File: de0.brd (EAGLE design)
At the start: 150.3 x 89.5 mm, 135 parts, among them IC1 PL2303SA__LF, J2 UX60SC-MB-5ST, U1 P0082, U2 RFM95W-915S2, U3 TPS76201DBVR, U4 TPS76201DBVR, U5 TPS76201DBVR

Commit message: change as Duran's suggest
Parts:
- removed U$48, U$49, U$50, U$51, U$52, U$53: (no value), qfp160:POINT
- added D10, D11, D12, D13, D14: LED0, SparkFun-LED:LED-0603
- added JP1, JP2, JP3: (no value), jumper:JP1
- added Q1, Q2, Q3, Q4, Q5: AS9013-H-HF, SamacSys_Parts:SOT95P240X105-3N
- added R23, R24, R25, R26, R27: 330, SparkFun-Resistors:0603
- added SV3, SV4: (no value), con-lstb:MA06-1
- REG_OUT_33: value REG_OUT_33 -> (none); device jumper:04C -> jumper:JP2Q
- moved C12 26.4 mm to (36.0, 44.2), flipped to the top, turned to 90 degrees
- moved C11 25.5 mm to (34.5, 44.3), flipped to the top, turned to 90 degrees
- moved C13 24.4 mm to (57.6, -3.56), flipped to the top, turned to 270 degrees
- moved C15 24.3 mm to (60.6, -3.55), flipped to the top, turned to 270 degrees
- moved C14 22.7 mm to (59.1, -3.55), flipped to the top, turned to 270 degrees
- moved C16 22.4 mm to (62.1, -3.57), flipped to the top, turned to 270 degrees
- moved C22 19.6 mm to (77.4, 44.1), flipped to the top
- moved C19 19.5 mm to (75.9, 44.1), flipped to the top
- moved REG_OUT_07 6.61 mm to (-22.9, 32.6)
- moved C21 6.07 mm to (59.0, 44.0), flipped to the top
- moved C17 6.03 mm to (60.3, 44.1), flipped to the top
- moved C20 5.95 mm to (61.8, 44.0), flipped to the top
- moved C18 5.48 mm to (63.4, 43.9), flipped to the top
- moved REG_OUT_33 4.58 mm to (-23.0, 13.4), turned to 270 degrees
- moved REG_OUT_12 4.36 mm to (-23.2, 23.4)
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- renumbered S1 to SW2, S2 to SW1, S3 to SW0, S4 to RESET, S5 to SW3, S6 to LOCKED
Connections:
- new net LORA_ANT: SV4.6, U2.9
- new net LORA_DIO1: SV4.2, U2.15
- new net LORA_DIO2: SV4.1, U2.16
- new net LORA_DIO3: SV4.5, U2.11
- new net LORA_DIO4: SV4.4, U2.12
- new net LORA_DIO5: SV3.6, U2.7
- new net N$10: D10.C, Q1.3
- new net N$11: D11.A, R24.1
- new net N$12: D11.C, Q2.3
- new net N$13: D12.A, R25.1
- new net N$14: D12.C, Q3.3
- new net N$15: D13.A, R26.1
- new net N$16: D13.C, Q4.3
- new net N$18: D14.A, R27.1
- new net N$19: D14.C, Q5.3
- new net N$23: JP1.2, R8.2
- new net N$24: JP2.2, R7.2
- new net N$25: JP3.2, R6.2
- new net N$9: D10.A, R23.1
- net GND: now also Q1.2, Q2.2, Q3.2, Q4.2, Q5.2
- net LORA_DIO0: now also JP1.1, SV4.3; no longer R8.2, U$53.1
- net LORA_MISO: now also SV3.1; no longer U$48.1
- net LORA_MOSI: now also SV3.2; no longer U$49.1
- net LORA_NSS: now also JP3.1, SV3.4; no longer R6.2, U$51.1
- net LORA_RESET: now also JP2.1, SV3.5; no longer R7.2, U$52.1
- net LORA_SCK: now also SV3.3; no longer U$50.1
- net OUT_33: now also REG_OUT_33.3; no longer REG_OUT_33.1
- net VCCQ: now also Q3.1
- net VO_07: now also Q4.1
- net VO_12: now also Q5.1
- net VO_33: now also Q1.1, REG_OUT_33.4
- net VO_FPGA_33: now also Q2.1, R23.2, R24.2, R25.2, R26.2, R27.2, REG_OUT_33.1; no longer REG_OUT_33.3
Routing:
- net GND: track 202.4 -> 298.7 mm
- net VO_FPGA_33: track 53.5 -> 0.00 mm
- net ADDRESS_10: track 56.1 -> 4.86 mm
- net VO_33: track 195.1 -> 156.9 mm
- net INTERRUPTS_6: track 123.1 -> 94.5 mm
- net VDDH: track 80.9 -> 58.5 mm, vias 7 -> 8
- net INTERRUPTS_5: track 136.7 -> 114.6 mm
- net VDDLS: track 90.6 -> 72.4 mm
- net VO_12: track 34.0 -> 17.2 mm
- net VCCQ: track 139.6 -> 124.2 mm, vias 13 -> 6
- net VO_07: track 28.3 -> 14.0 mm
- net VBN: track 62.7 -> 49.7 mm
- net OUT_07: track 16.6 -> 5.78 mm
- net LORA_NSS: track 52.8 -> 43.7 mm
- net ADDRESS_11: track 59.8 -> 51.6 mm
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- removed copper zone on layer 1, net GND
- removed copper zone on layer 16, net GND
- removed copper zone on layer 1, net OUT_07
- removed copper zone on layer 1, net OUT_12
- removed copper zone on layer 1, net OUT_33
- removed copper zone on layer 1, net VO_07

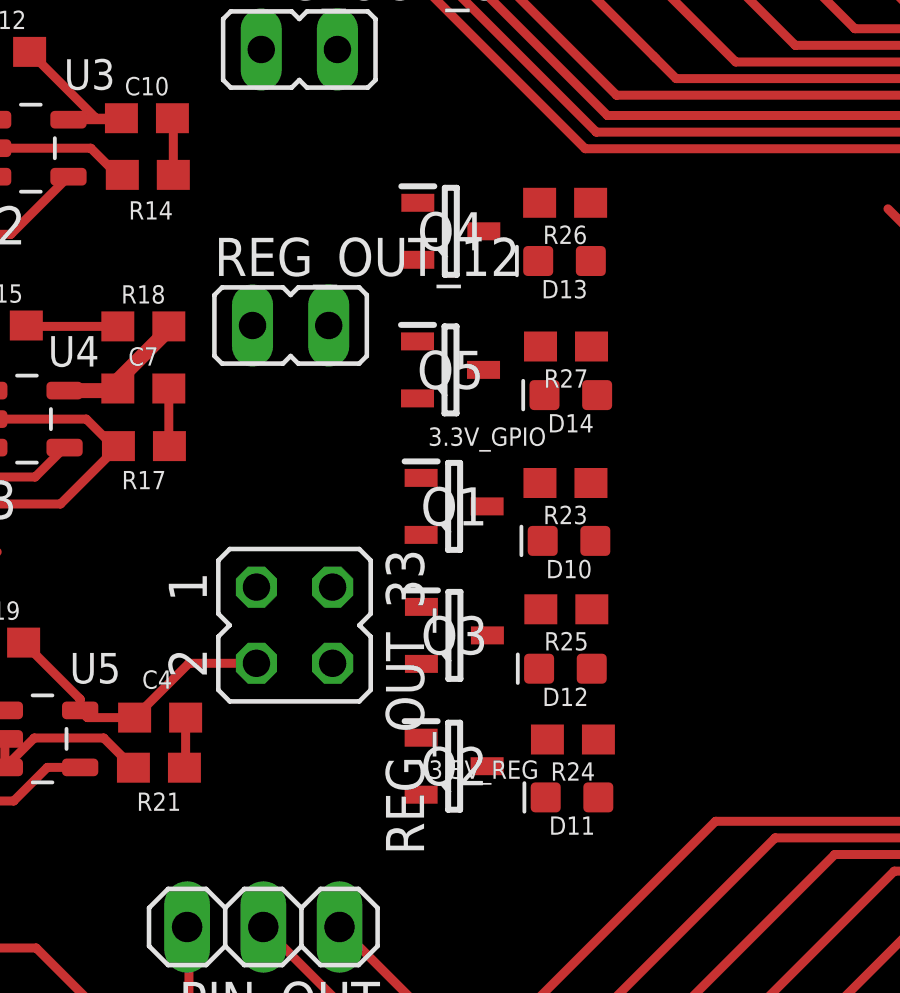
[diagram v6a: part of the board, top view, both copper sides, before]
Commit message: change BJT to MOSFET for power leds
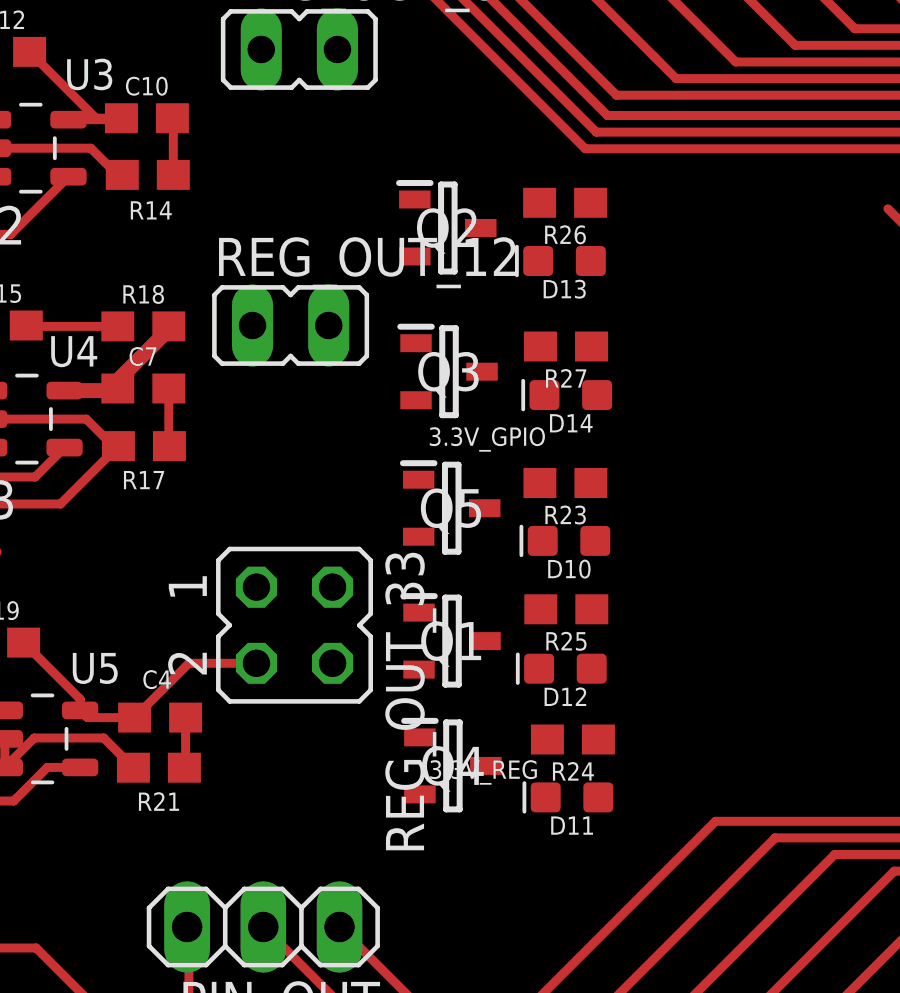
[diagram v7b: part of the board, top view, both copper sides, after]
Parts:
- Q1, Q2, Q3, Q4, Q5: value AS9013-H-HF -> BSH103,235; device SamacSys_Parts:SOT95P240X105-3N -> SamacSys_Parts:SOT95P230X110-3N
- moved Q2 17.9 mm to (-17.9, 26.6)
- moved Q4 17.8 mm to (-17.8, 8.72)
- moved Q3 8.79 mm to (-17.9, 21.9)
- moved Q5 4.61 mm to (-17.8, 17.3)
- moved Q1 4.49 mm to (-17.8, 12.9)
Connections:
- net N$10: now also Q5.3; no longer Q1.3
- net N$12: now also Q4.3; no longer Q2.3
- net N$14: now also Q1.3; no longer Q3.3
- net N$16: now also Q2.3; no longer Q4.3
- net N$19: now also Q3.3; no longer Q5.3
- net OUT_33: now also Q5.1
- net VCCQ: now also Q1.1; no longer Q3.1
- net VO_07: now also Q3.1; no longer Q4.1
- net VO_12: now also Q2.1; no longer Q5.1
- net VO_33: no longer Q1.1
- net VO_FPGA_33: now also Q4.1; no longer Q2.1

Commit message: Update again with Duran's suggest
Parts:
- removed JP1, JP2, JP3: (no value), jumper:JP1
- removed REG_OUT_07: REG_OUT_07, jumper:JP1
- added H1, H2, H3, H4: MOUNT-HOLE3.3, holes:3,3
- added J1: (no value), SparkFun-Connectors:1X02
- added LORA_DIO0, LORA_NSS, LORA_RESET: (no value), jumper:JP1
- added OUT_07: REG_OUT_07, jumper:JP1
- moved C11 32.3 mm to (17.4, 16.8), turned to 180 degrees
- moved C12 31.8 mm to (17.4, 18.4), turned to 180 degrees
- moved C13 21.1 mm to (36.6, -5.23)
- moved C14 21.1 mm to (38.1, -5.22)
- moved C15 20.2 mm to (40.4, -5.22)
- moved C16 20.2 mm to (41.9, -5.24)
- moved Q4 15.6 mm to (-10.8, 22.6)
- moved Q2 15.3 mm to (-10.7, 13.2)
- moved Q5 12.0 mm to (-10.7, 27.0)
- moved D10 10.8 mm to (-6.86, 8.02)
- moved R23 10.8 mm to (-6.98, 9.95)
- moved LOCKED 9.65 mm to (40.8, -31.8)
- moved RESET 9.53 mm to (48.4, -31.8)
- moved R27 8.95 mm to (-6.83, 28.1)
- moved D12 8.70 mm to (-6.76, 16.8)
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- renumbered 5V_JUMPER to 5V, REG_IN_07 to IN_07, REG_IN_12 to IN_12, REG_IN_33 to IN_33, REG_OUT_12 to OUT_12, REG_OUT_33 to OUT_33, UART_JUMPER to UART
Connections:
- net LOCKED: now also J1.1
- net LORA_DIO0: now also LORA_DIO0.1; no longer JP1.1
- net LORA_NSS: now also LORA_NSS.1; no longer JP3.1
- net LORA_RESET: now also LORA_RESET.1; no longer JP2.1
- net N$10: now also Q1.3; no longer Q5.3
- net N$12: now also D12.C, Q3.3; no longer D11.C, Q4.3
- net N$14: now also D11.C, Q2.3; no longer D12.C, Q1.3
- net N$16: now also Q4.3; no longer Q2.3
- net N$19: now also Q5.3; no longer Q3.3
- net N$23: now also LORA_DIO0.2; no longer JP1.2
- net N$24: now also LORA_RESET.2; no longer JP2.2
- net N$25: now also LORA_NSS.2; no longer JP3.2
- net OUT_07: now also OUT_07.1; no longer REG_OUT_07.1
- net OUT_33: now also Q1.1; no longer Q5.1
- net RESET: now also J1.2
- net VCCQ: no longer Q1.1
- net VO_07: now also OUT_07.2, Q5.1; no longer Q3.1, REG_OUT_07.2
- net VO_12: now also Q4.1; no longer Q2.1
- net VO_33: now also Q2.1, R23.2, R24.2, R25.2, R26.2, R27.2
- net VO_FPGA_33: now also Q3.1; no longer Q4.1, R23.2, R24.2, R25.2, R26.2, R27.2
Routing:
- net GND: track 298.7 -> 457.3 mm, vias 47 -> 405
- net VO_FPGA_33: track 0.00 -> 74.1 mm, vias 0 -> 6
- net VO_33: track 156.9 -> 225.0 mm
- net VDDLS: track 72.4 -> 121.6 mm
- net ADDRESS_10: track 4.86 -> 53.4 mm
- net VDDH: track 58.5 -> 99.0 mm, vias 8 -> 3
- net VO_12: track 17.2 -> 51.0 mm, vias 4 -> 3
- net VCCQ: track 124.2 -> 153.6 mm, vias 6 -> 0
- net INTERRUPTS_6: track 94.5 -> 123.0 mm
- net RESET: track 72.2 -> 99.8 mm, vias 0 -> 2
- net VO_07: track 14.0 -> 37.4 mm, vias 0 -> 3
- net VBN: track 49.7 -> 72.9 mm, vias 0 -> 3
- net INTERRUPTS_5: track 114.6 -> 136.5 mm
- net ADDRESS_3: track 76.7 -> 95.9 mm, vias 0 -> 1
- net LORA_NSS: track 43.7 -> 58.8 mm
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- added copper zone on layer 1, net GND
- added copper zone on layer 16, net GND
- added copper zone on layer 1, net OUT_07
- added copper zone on layer 1, net OUT_12
- added copper zone on layer 1, net OUT_33
- added copper zone on layer 1, net VBN
- added copper zone on layer 1, net VO_07
- added copper zone on layer 16, net VO_07
- added copper zone on layer 1, net VO_FPGA_33
- added copper zone on layer 16, net VO_FPGA_33
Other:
- board size 150.3 x 89.5 mm -> 150.3 x 98.4 mm
- board text added: "GND"
- board text added: "LOCKED"
- board text added: "LORA_ANT"
- board text added: "LORA_DIO1"
- board text added: "LORA_DIO2"
- board text added: "LORA_DIO3"
- board text added: "LORA_DIO4"
- board text added: "LORA_DIO5"
- board text added: "OPEN8 Demo Kit"
- board text added: "RESET"
- board text added: "RX"
- board text added: "SOTB v1.0 UEC Pham Lab 2021"
- board text added: "SPI_CS"
- board text added: "SPI_MISO"
- board text added: "SPI_MOSI"
- board text added: "SPI_SCK"
- board text added: "TX"
- board text added: "bottom"
- board text added: "top"
